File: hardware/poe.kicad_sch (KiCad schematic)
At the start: 54 parts, among them T2 HR051067, U10 EL357N(B)(TA)-G, U11 CJ431, U9 Si3402-B

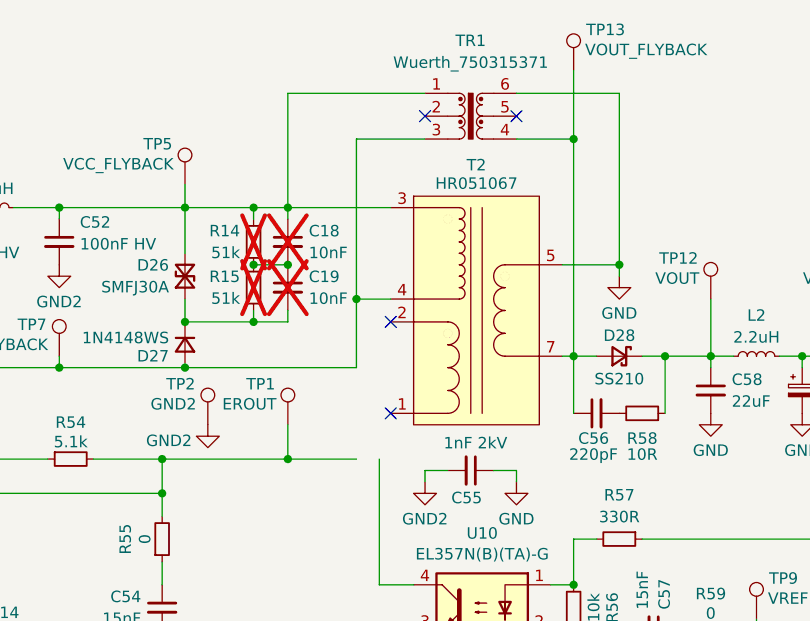
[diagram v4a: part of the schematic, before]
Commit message: hardware: add LCSC partnumber to ESP32-C3 module
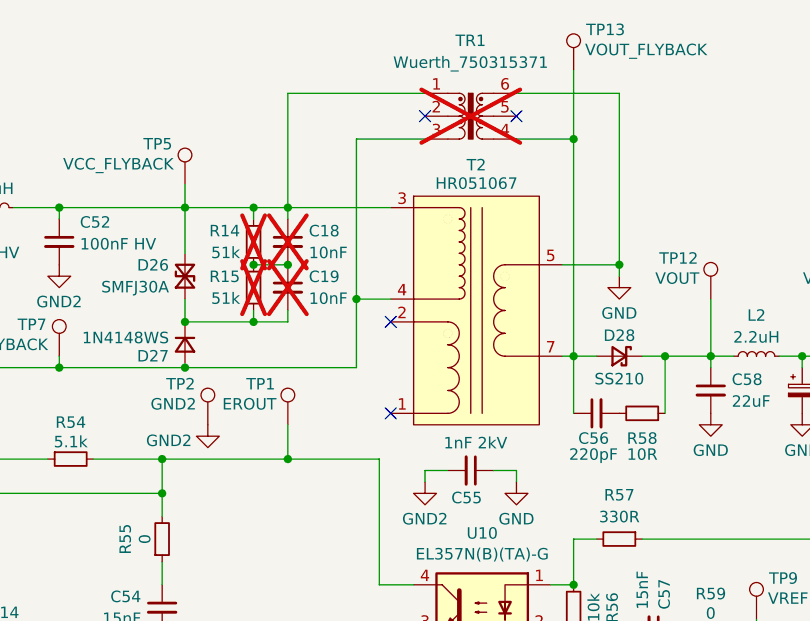
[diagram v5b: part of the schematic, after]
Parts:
- TR1: now not fitted
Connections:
- net at U10.4: now also R54.2, R55.2, TP1.1, U9.1 (EROUT)
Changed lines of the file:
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@@
 	(wire
 		(pts
-			(xy 162.56 104.14) (xy 170.18 104.14)
+			(xy 162.56 104.14) (xy 172.72 104.14)
 		)
 		(stroke
@@
 		(in_bom yes)
 		(on_board yes)
-		(dnp no)
+		(dnp yes)
 		(property "Reference" "TR1"
 			(at 182.88 57.658 0)

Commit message: Implement review comments by Urmel
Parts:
- C57: value 15nF -> 1nF; LCSC C15195 -> C1523
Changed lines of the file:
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@@
 			)
 		)
-		(property "Value" "15nF"
+		(property "Value" "1nF"
 			(at 201.9816 120.8659 0)
 			(effects
@@
 			)
 		)
-		(property "LCSC" "C15195"
+		(property "LCSC" "C1523"
 			(at 203.2 123.19 0)
 			(effects

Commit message: Exclude parts with virtual footprints from BOM
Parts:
- C18, C19, R14, R15, TP1, TP10, TP11, TP12, TP13, TP14, TP2, TP23, TP3, TP4, TP5, TP6, TP7, TP8, TP9, TR1: now left out of the parts list
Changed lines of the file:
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@@
 		(unit 1)
 		(exclude_from_sim no)
-		(in_bom yes)
+		(in_bom no)
 		(on_board yes)
 		(dnp no)
@@
 		(unit 1)
 		(exclude_from_sim no)
-		(in_bom yes)
+		(in_bom no)
 		(on_board yes)
 		(dnp no)
@@
 		(unit 1)
 		(exclude_from_sim no)
-		(in_bom yes)
+		(in_bom no)
 		(on_board yes)
 		(dnp no)
@@
 		(unit 1)
 		(exclude_from_sim no)
-		(in_bom yes)
+		(in_bom no)
 		(on_board yes)
 		(dnp yes)
@@
 		(unit 1)
 		(exclude_from_sim no)
-		(in_bom yes)
+		(in_bom no)
 		(on_board yes)
 		(dnp no)
@@
 		(unit 1)
 		(exclude_from_sim no)
-		(in_bom yes)
+		(in_bom no)
 		(on_board yes)
 		(dnp no)
@@
 		(unit 1)
 		(exclude_from_sim no)
-		(in_bom yes)
+		(in_bom no)
 		(on_board yes)
 		(dnp yes)
@@
 		(unit 1)
 		(exclude_from_sim no)
-		(in_bom yes)
+		(in_bom no)
 		(on_board yes)
 		(dnp no)
@@
 		(unit 1)
 		(exclude_from_sim no)
-		(in_bom yes)
+		(in_bom no)
 		(on_board yes)
 		(dnp no)
@@
 		(unit 1)
 		(exclude_from_sim no)
-		(in_bom yes)
+		(in_bom no)
 		(on_board yes)
 		(dnp no)
@@
 		(unit 1)
 		(exclude_from_sim no)
-		(in_bom yes)
+		(in_bom no)
 		(on_board yes)
 		(dnp no)
@@
 		(unit 1)
 		(exclude_from_sim no)
-		(in_bom yes)
+		(in_bom no)
 		(on_board yes)
 		(dnp yes)
@@
 		(unit 1)
 		(exclude_from_sim no)
-		(in_bom yes)
+		(in_bom no)
 		(on_board yes)
 		(dnp yes)
@@
 		(unit 1)
 		(exclude_from_sim no)
-		(in_bom yes)
+		(in_bom no)
 		(on_board yes)
 		(dnp no)
@@
 		(unit 1)
 		(exclude_from_sim no)
-		(in_bom yes)
+		(in_bom no)
 		(on_board yes)
 		(dnp yes)
@@
 		(unit 1)
 		(exclude_from_sim no)
-		(in_bom yes)
+		(in_bom no)
 		(on_board yes)
 		(dnp no)
@@
 		(unit 1)
 		(exclude_from_sim no)
-		(in_bom yes)
+		(in_bom no)
 		(on_board yes)
 		(dnp no)
@@
 		(unit 1)
 		(exclude_from_sim no)
-		(in_bom yes)
+		(in_bom no)
 		(on_board yes)
 		(dnp no)
@@
 		(unit 1)
 		(exclude_from_sim no)
-		(in_bom yes)
+		(in_bom no)
 		(on_board yes)
 		(dnp no)
@@
 		(unit 1)
 		(exclude_from_sim no)
-		(in_bom yes)
+		(in_bom no)
 		(on_board yes)
 		(dnp no)

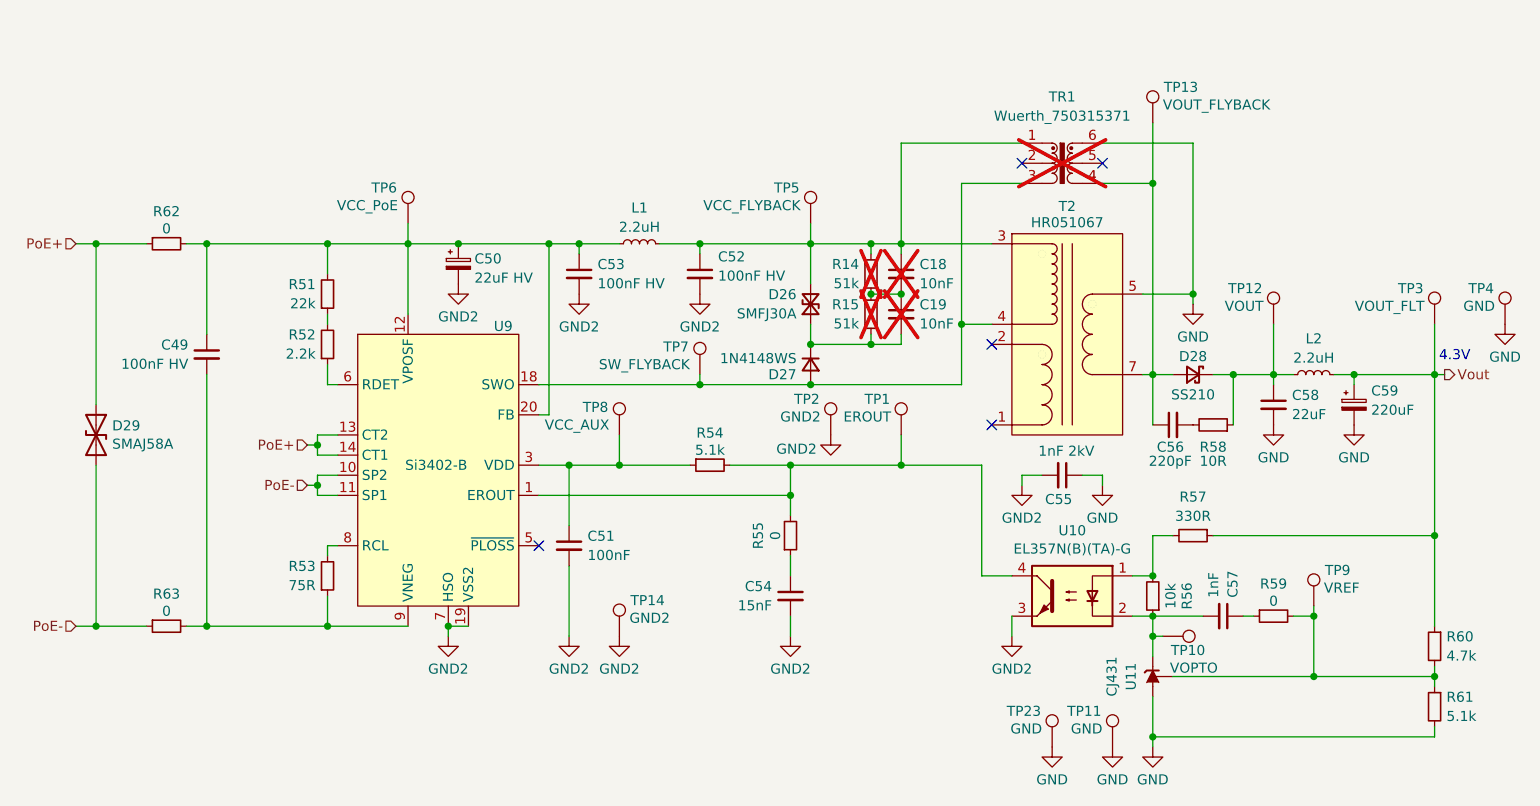
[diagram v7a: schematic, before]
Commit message: Optimize flyback feedback loop stability
During load testing on an initial prototype better component values for the
flyback feedback loop were found. Update design with those.
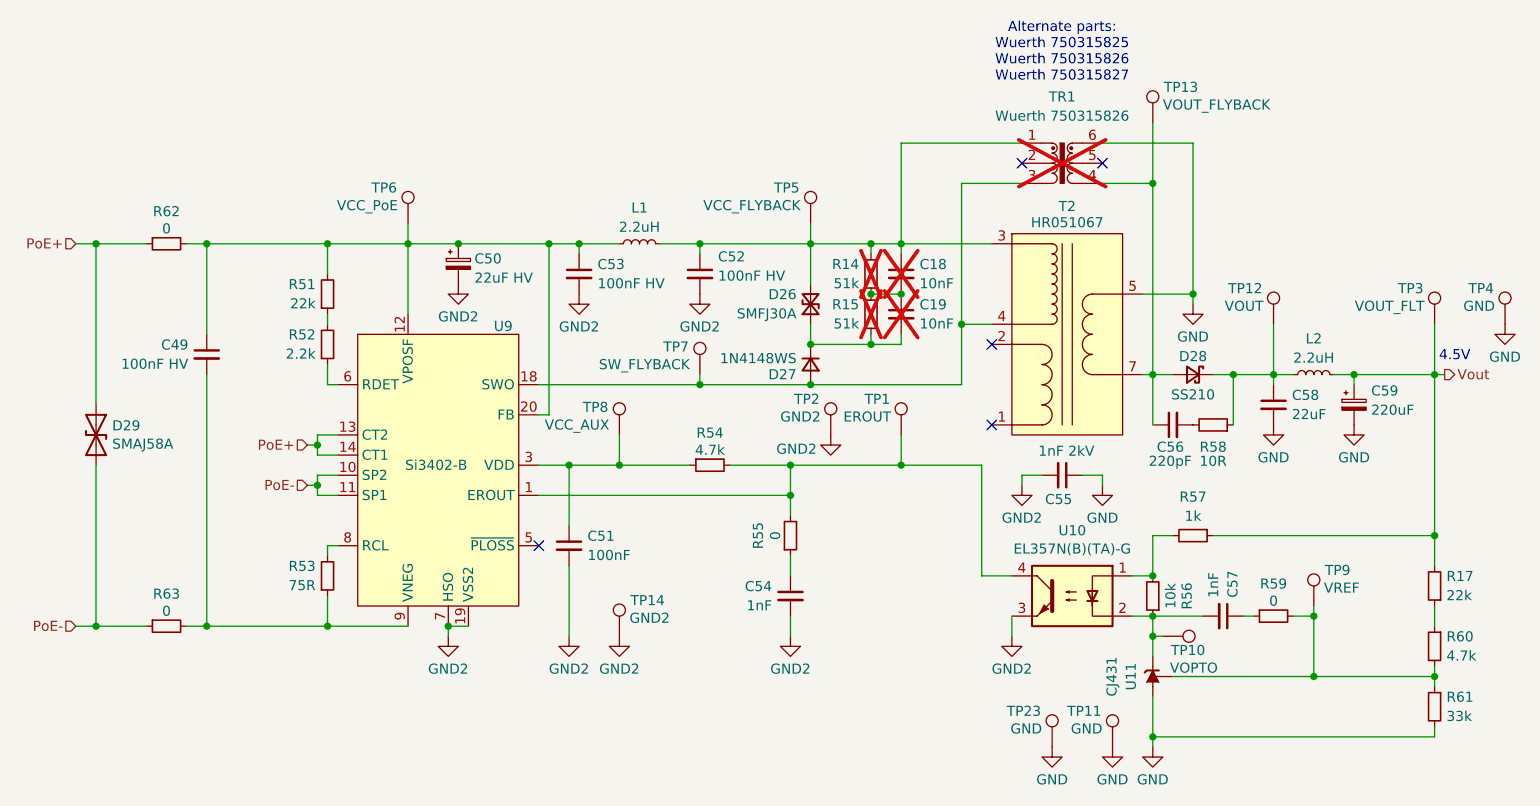
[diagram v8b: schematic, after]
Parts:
- added R17: 22k, Resistor_SMD:R_0402_1005Metric, symbol Device:R_Small
- C54: value 15nF -> 1nF; LCSC C15195 -> C1523
- R54: value 5.1k -> 4.7k; LCSC C25905 -> C25900
- R57: value 330R -> 1k; LCSC C25104 -> C11702
- R61: value 5.1k -> 33k; LCSC C25905 -> C25779
- TR1: value Wuerth_750315371 -> Wuerth 750315826
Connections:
- net Vout: now also R17.2; no longer R60.1
- new net: R17.1, R60.1
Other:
- note added: "4.5V"
- note added: "Alternate parts: Wuerth 750315825 Wuerth 750315826 Wuerth 750315827"
- note removed: "4.3V"
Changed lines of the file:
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@@
 	)
 	(junction
-		(at 229.87 113.03)
-		(diameter 0)
-		(color 0 0 0 0)
-	)
-	(junction
 		(at 170.18 86.36)
 		(diameter 0)
@@
 	)
 	(junction
+		(at 229.87 113.03)
+		(diameter 0)
+		(color 0 0 0 0)
+	)
+	(junction
 		(at 158.75 88.9)
 		(diameter 0)
@@
 	(wire
 		(pts
+			(xy 229.87 121.92) (xy 229.87 124.46)
+		)
+		(stroke
+			(width 0)
+			(type default)
+		)
+	)
+	(wire
+		(pts
 			(xy 162.56 88.9) (xy 162.56 87.63)
 		)
@@
 	(wire
 		(pts
+			(xy 229.87 113.03) (xy 229.87 116.84)
+		)
+		(stroke
+			(width 0)
+			(type default)
+		)
+	)
+	(wire
+		(pts
 			(xy 60.96 104.14) (xy 60.96 124.46)
 		)
@@
 	(wire
 		(pts
-			(xy 229.87 113.03) (xy 229.87 124.46)
-		)
-		(stroke
-			(width 0)
-			(type default)
-		)
-	)
-	(wire
-		(pts
 			(xy 90.17 114.3) (xy 90.17 115.57)
 		)
@@
 		)
 	)
-	(text "4.3V"
+	(text "4.5V"
 		(exclude_from_sim no)
 		(at 232.41 90.424 0)
@@
 		)
 	)
+	(text "Alternate parts:\nWuerth 750315825\nWuerth 750315826\nWuerth 750315827"
+		(exclude_from_sim no)
+		(at 182.88 52.07 0)
+		(effects
+			(font
+				(size 1.27 1.27)
+			)
+		)
+	)
 	(hierarchical_label "PoE-"
 		(shape input)
@@
 			)
 		)
-		(property "Value" "330R"
+		(property "Value" "1k"
 			(at 199.39 110.5732 90)
 			(effects
@@
 			)
 		)
-		(property "LCSC" "C25104"
+		(property "LCSC" "C11702"
 			(at 199.39 113.03 0)
 			(effects
@@
 	(symbol
 		(lib_id "Device:R_Small")
+		(at 229.87 119.38 180)
+		(unit 1)
+		(exclude_from_sim no)
+		(in_bom yes)
+		(on_board yes)
+		(dnp no)
+		(property "Reference" "R17"
+			(at 231.3686 118.1678 0)
+			(effects
+				(font
+					(size 1.27 1.27)
+				)
+				(justify right)
+			)
+		)
+		(property "Value" "22k"
+			(at 231.3686 120.5921 0)
+			(effects
+				(font
+					(size 1.27 1.27)
+				)
+				(justify right)
+			)
+		)
+		(property "Footprint" "Resistor_SMD:R_0402_1005Metric"
+			(at 229.87 119.38 0)
+			(effects
+				(font
+					(size 1.27 1.27)
+				)
+				(hide yes)
+			)
+		)
+		(property "Datasheet" "~"
+			(at 229.87 119.38 0)
+			(effects
+				(font
+					(size 1.27 1.27)
+				)
+				(hide yes)
+			)
+		)
+		(property "Description" "Resistor, small symbol"
+			(at 229.87 119.38 0)
+			(effects
+				(font
+					(size 1.27 1.27)
+				)
+				(hide yes)
+			)
+		)
+		(property "LCSC" "C25768"
+			(at 229.87 119.38 0)
+			(effects
+				(font
+					(size 1.27 1.27)
+				)
+				(hide yes)
+			)
+		)
+		(pin "2"
+		)
+		(pin "1"
+		)
+		(instances
+			(project "TallyLight"
+				(path "/d4f869dd-5485-4b4f-b239-21313c2a8e4c/210de0db-26c5-4c02-8853-8d735ccb28a9"
+					(reference "R17")
+					(unit 1)
+				)
+			)
+		)
+	)
+	(symbol
+		(lib_id "Device:R_Small")
 		(at 229.87 134.62 0)
 		(mirror y)
@@
 			)
 		)
-		(property "Value" "5.1k"
+		(property "Value" "33k"
 			(at 231.3686 135.8321 0)
 			(effects
@@
 			)
 		)
-		(property "LCSC" "C25905"
+		(property "LCSC" "C25779"
 			(at 229.87 134.62 0)
 			(effects
@@
 			)
 		)
-		(property "Value" "Wuerth_750315371"
+		(property "Value" "Wuerth 750315826"
 			(at 182.88 60.0823 0)
 			(effects
@@
 			)
 		)
-		(property "Value" "5.1k"
+		(property "Value" "4.7k"
 			(at 138.43 102.2405 90)
 			(effects
@@
 			)
 		)
-		(property "LCSC" "C25905"
+		(property "LCSC" "C25900"
 			(at 138.43 104.14 0)
 			(effects
@@
 			)
 		)
-		(property "Value" "15nF"
+		(property "Value" "1nF"
 			(at 146.2659 121.8684 0)
 			(effects
@@
 			)
 		)
-		(property "LCSC" "C15195"
+		(property "LCSC" "C1523"
 			(at 148.59 120.65 0)
 			(effects
